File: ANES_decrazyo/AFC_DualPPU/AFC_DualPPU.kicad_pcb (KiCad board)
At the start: 2 copper layers, 72.4 x 76.8 mm, 14 parts, among them J1 RP2C02G PPU Socket, J2 A12, J3 74LS139 Socket, U1 74LS139 #2, U2 74LS373 #2, U3 74LS139 #1, U4 6264 VRAM#2, U5A1 RP2C02G PPU #1, U5B1 RP2C02G PPU #2

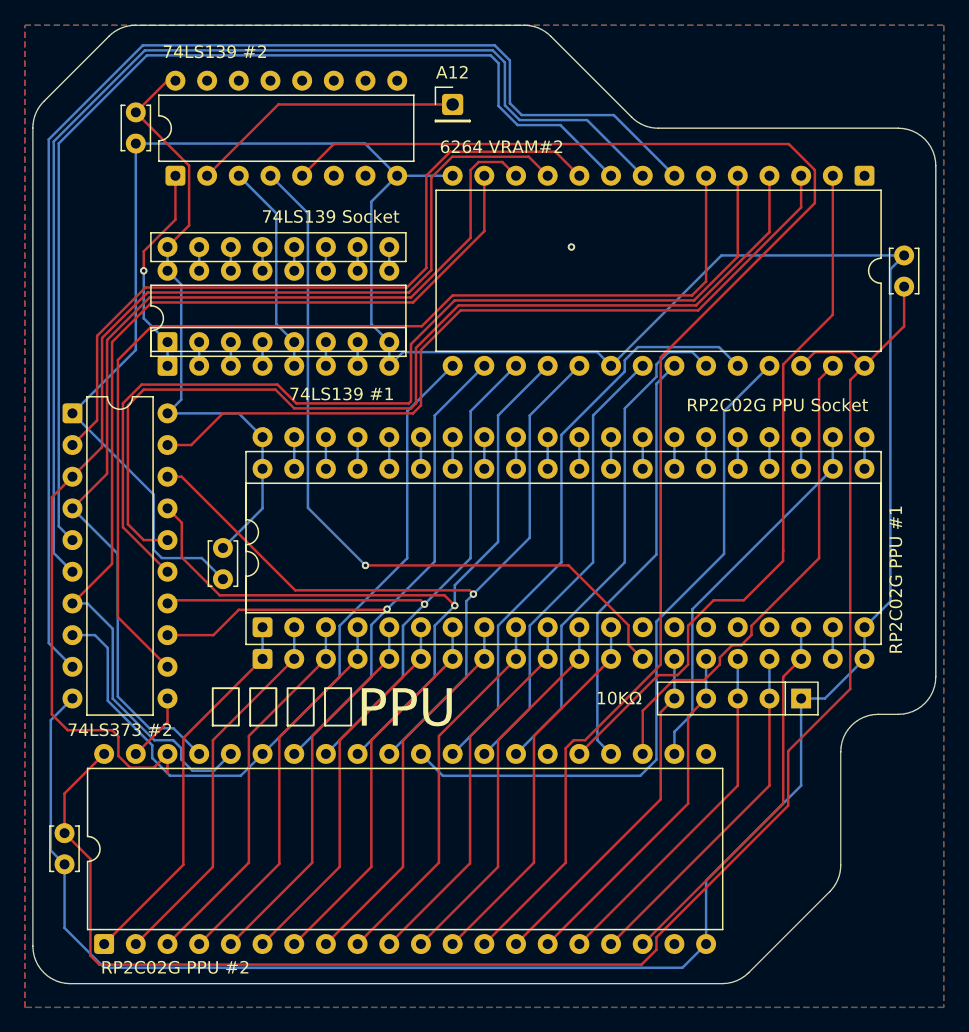
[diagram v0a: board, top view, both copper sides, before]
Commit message: Moved decoupling capacitor
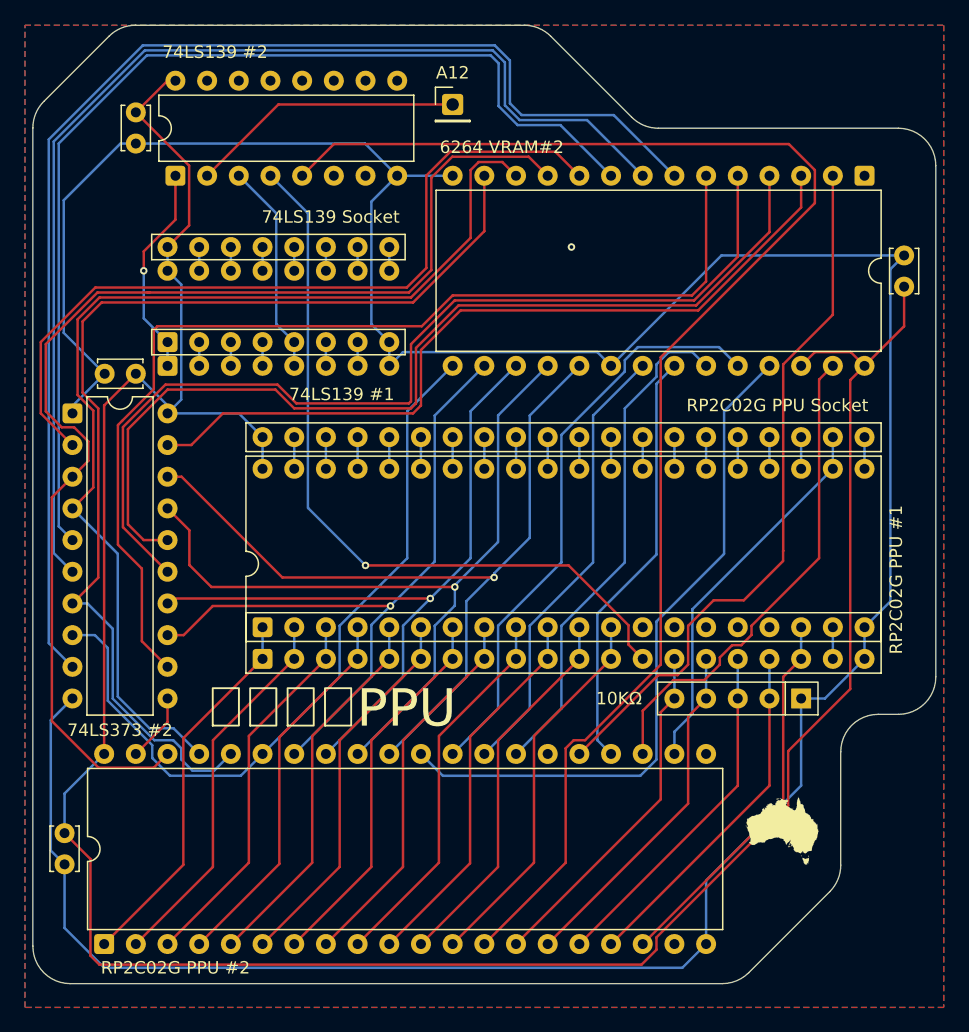
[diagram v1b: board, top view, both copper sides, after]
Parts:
- moved C2 15.6 mm to (150.5, 62.9), turned to 180 degrees
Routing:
- net +5V: track 182.3 -> 210.4 mm
- net GND: track 268.9 -> 252.2 mm
- net /O0: track 59.5 -> 63.9 mm
- net PPU2_AD0: track 92.5 -> 96.3 mm
- net PPU2_AD1: track 82.0 -> 85.4 mm
- net PPU2_AD2: track 82.9 -> 86.3 mm
- net PPU2_AD7: track 65.8 -> 67.2 mm
- net /O5: track 79.6 -> 78.5 mm
- net /O6: track 78.8 -> 77.7 mm
- net PPU2_AD6: track 65.3 -> 64.7 mm
